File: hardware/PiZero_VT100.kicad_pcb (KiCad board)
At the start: 2 copper layers, 99.8 x 100.1 mm, 41 parts, among them J1 GPIO, J2 RS232, J3 Ext. Power max,. 9V DC/AC, J4 Mini-DIN-6, J5 to Testpins 22(DM) and TP23(D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, J6 USB_A, J7 Z80-MBC2 direct, J8 LCD Power, J9 On / Off, K1 G5V-2, Q1 BC546, Q2 BC546, U1 LM350_TO220

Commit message: small changes, typos
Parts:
- moved J8 38.6 mm to (136.7, 118.1), turned to 0 degrees
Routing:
- net +5V: track 295.6 -> 299.7 mm
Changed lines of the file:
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@@
 		(grid_origin 99.2 168.6)
 		(pcbplotparams
-			(layerselection 0x00000000_00000000_55555555_57555554)
+			(layerselection 0x00000000_00000000_5555555d_df55557f)
 			(plot_on_all_layers_selection 0x00000000_00000000_00000000_00000000)
 			(disableapertmacros no)
@@
 	(footprint "Connector_PinHeader_2.54mm:PinHeader_1x02_P2.54mm_Vertical"
 		(layer "F.Cu")
-		(at 105.775 95 -90)
+		(at 136.7 118.075)
 		(descr "Through hole straight pin header, 1x02, 2.54mm pitch, single row")
 		(tags "Through hole pin header THT 1x02 2.54mm single row")
 		(property "Reference" "J8"
-			(at 0 -2.38 90)
+			(at 0 -2.38 0)
 			(layer "F.SilkS")
 			(effects
@@
 		)
 		(property "Value" "LCD Power"
-			(at -3.5 0.775 180)
+			(at -3.5 0.775 90)
 			(layer "F.Fab")
 			(effects
@@
 		)
 		(property "Datasheet" ""
-			(at 0 0 90)
+			(at 0 0 0)
 			(layer "F.Fab")
 			(hide yes)
@@
 		)
 		(property "Description" "Generic connector, single row, 01x02, script generated"
-			(at 0 0 90)
+			(at 0 0 0)
 			(layer "F.Fab")
 			(hide yes)
@@
 		(attr through_hole)
 		(fp_line
-			(start -1.38 3.92)
-			(end 1.38 3.92)
+			(start -1.38 -1.38)
+			(end 0 -1.38)
 			(stroke
 				(width 0.12)
@@
 		)
 		(fp_line
-			(start -1.38 1.27)
-			(end -1.38 3.92)
+			(start -1.38 0)
+			(end -1.38 -1.38)
 			(stroke
 				(width 0.12)
@@
 		(fp_line
 			(start -1.38 1.27)
-			(end 1.38 1.27)
+			(end -1.38 3.92)
 			(stroke
 				(width 0.12)
@@
 		)
 		(fp_line
-			(start 1.38 1.27)
-			(end 1.38 3.92)
+			(start -1.38 1.27)
+			(end 1.38 1.27)
 			(stroke
 				(width 0.12)
@@
 		)
 		(fp_line
-			(start -1.38 0)
-			(end -1.38 -1.38)
+			(start -1.38 3.92)
+			(end 1.38 3.92)
 			(stroke
 				(width 0.12)
@@
 		)
 		(fp_line
-			(start -1.38 -1.38)
-			(end 0 -1.38)
+			(start 1.38 1.27)
+			(end 1.38 3.92)
 			(stroke
 				(width 0.12)
@@
 		)
 		(fp_line
-			(start -1.77 4.32)
-			(end 1.77 4.32)
+			(start -1.77 -1.77)
+			(end -1.77 4.32)
 			(stroke
 				(width 0.05)
@@
 		)
 		(fp_line
-			(start 1.77 4.32)
-			(end 1.77 -1.77)
+			(start -1.77 4.32)
+			(end 1.77 4.32)
 			(stroke
 				(width 0.05)
@@
 		)
 		(fp_line
-			(start -1.77 -1.77)
-			(end -1.77 4.32)
+			(start 1.77 -1.77)
+			(end -1.77 -1.77)
 			(stroke
 				(width 0.05)
@@
 		)
 		(fp_line
-			(start 1.77 -1.77)
-			(end -1.77 -1.77)
+			(start 1.77 4.32)
+			(end 1.77 -1.77)
 			(stroke
 				(width 0.05)
@@
 		)
 		(fp_line
-			(start -1.27 3.81)
-			(end -1.27 -0.635)
+			(start -1.27 -0.635)
+			(end -0.635 -1.27)
 			(stroke
 				(width 0.1)
@@
 		)
 		(fp_line
-			(start 1.27 3.81)
-			(end -1.27 3.81)
+			(start -1.27 3.81)
+			(end -1.27 -0.635)
 			(stroke
 				(width 0.1)
@@
 		)
 		(fp_line
-			(start -1.27 -0.635)
-			(end -0.635 -1.27)
+			(start -0.635 -1.27)
+			(end 1.27 -1.27)
 			(stroke
 				(width 0.1)
@@
 		)
 		(fp_line
-			(start -0.635 -1.27)
-			(end 1.27 -1.27)
+			(start 1.27 -1.27)
+			(end 1.27 3.81)
 			(stroke
 				(width 0.1)
@@
 		)
 		(fp_line
-			(start 1.27 -1.27)
-			(end 1.27 3.81)
+			(start 1.27 3.81)
+			(end -1.27 3.81)
 			(stroke
 				(width 0.1)
@@
 		)
 		(fp_text user "${REFERENCE}"
-			(at 0 1.27 0)
+			(at 0 1.27 90)
 			(layer "F.Fab")
 			(effects
@@
 		)
 		(pad "1" thru_hole rect
-			(at 0 0 270)
+			(at 0 0)
 			(size 1.7 1.7)
 			(drill 1)
@@
 		)
 		(pad "2" thru_hole circle
-			(at 0 2.54 270)
+			(at 0 2.54)
 			(size 1.7 1.7)
 			(drill 1)
@@
 	)
 	(segment
+		(start 136.7 118.075)
+		(end 127.125 118.075)
+		(width 0.8)
+		(layer "B.Cu")
+		(net 30)
+	)
+	(segment
 		(start 135.91 148.05)
 		(end 130.96 143.1)
@@
 	)
 	(segment
-		(start 127 120)
+		(start 127 117.95)
 		(end 127 113.2)
 		(width 0.8)
@@
 	)
 	(segment
-		(start 105.775 98.942677)
-		(end 107 100.167677)
-		(width 0.8)
-		(layer "B.Cu")
-		(net 30)
-	)
-	(segment
 		(start 193 98)
 		(end 192 97)
@@
 	)
 	(segment
+		(start 127 120)
+		(end 127 117.95)
+		(width 0.8)
+		(layer "B.Cu")
+		(net 30)
+	)
+	(segment
 		(start 121.4 119.96)
 		(end 126.96 119.96)
@@
 	)
 	(segment
-		(start 105.775 95)
-		(end 105.775 98.942677)
+		(start 127.125 118.075)
+		(end 127 117.95)
 		(width 0.8)
 		(layer "B.Cu")

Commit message: Analyzing VT100 support and extension
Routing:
- net Net-(J3-Ext): track 14.8 -> 24.8 mm
- net +5V: track 299.7 -> 299.0 mm
- added copper zone on F.Cu, net GND
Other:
- board size 99.8 x 100.1 mm -> 99.7 x 99.6 mm
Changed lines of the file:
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@@
 			)
 		)
-		(pad "1" thru_hole circle
+		(pad "1" thru_hole rect
 			(at 0 0)
-			(size 2 2)
-			(drill 1.2)
+			(size 4.6 2)
+			(drill oval 3.6 1)
 			(layers "*.Cu" "*.Mask")
 			(remove_unused_layers no)
@@
 			(pintype "passive")
 		)
-		(pad "2" thru_hole circle
+		(pad "2" thru_hole oval
 			(at 0 6.3)
-			(size 2 2)
-			(drill 1.2)
+			(size 4.2 2)
+			(drill oval 3.2 1)
 			(layers "*.Cu" "*.Mask")
 			(remove_unused_layers no)
@@
 		(pad "3" thru_hole oval
 			(at 4.8 2.9)
-			(size 2 2)
-			(drill 1.2)
+			(size 2 4.2)
+			(drill oval 1 3.2)
 			(layers "*.Cu" "*.Mask")
 			(remove_unused_layers no)
@@
 	(gr_poly
 		(pts
-			(xy 99.15 68.5) (xy 198.95 68.5) (xy 198.95 168.55) (xy 187.498724 168.452955) (xy 187.548743 160.5)
+			(xy 99.1502 68.9) (xy 198.85 68.9) (xy 198.85 168.549152) (xy 187.498724 168.452955) (xy 187.548743 160.5)
 			(xy 173.5 160.5) (xy 173.50092 168.45) (xy 99.2 168.45)
 		)
@@
 	)
 	(segment
-		(start 106.917677 100.25)
-		(end 107.5 100.25)
-		(width 0.8)
-		(layer "B.Cu")
-		(net 30)
-	)
-	(segment
 		(start 192 97)
 		(end 183.5 97)
@@
 	)
 	(segment
-		(start 107 100.167677)
-		(end 106.917677 100.25)
-		(width 0.8)
-		(layer "B.Cu")
-		(net 30)
-	)
-	(segment
 		(start 112.5 143.5)
 		(end 109.5 146.5)
@@
 	)
 	(segment
-		(start 111.75 158.8)
-		(end 114.1 156.45)
+		(start 114.1 147.48)
+		(end 114.58 147)
 		(width 0.8)
 		(layer "B.Cu")
@@
 	)
 	(segment
-		(start 114.1 147.48)
-		(end 114.58 147)
+		(start 111.85 160.7)
+		(end 111.75 160.6)
+		(width 0.8)
+		(layer "B.Cu")
+		(net 36)
+	)
+	(segment
+		(start 114.58 147)
+		(end 115.5 147)
 		(width 0.8)
 		(layer "B.Cu")
@@
 	)
 	(segment
-		(start 111.75 160.6)
-		(end 111.75 158.8)
+		(start 115.5 147)
+		(end 119.55 151.05)
 		(width 0.8)
 		(layer "B.Cu")
@@
 	)
 	(segment
-		(start 114.1 156.45)
-		(end 114.1 147.48)
+		(start 119.55 151.05)
+		(end 119.55 160.7)
+		(width 0.8)
+		(layer "B.Cu")
+		(net 36)
+	)
+	(segment
+		(start 119.55 160.7)
+		(end 111.85 160.7)
 		(width 0.8)
 		(layer "B.Cu")
@@
 		(net 1)
 		(net_name "GND")
-		(layer "B.Cu")
+		(layers "F.Cu" "B.Cu")
 		(hatch edge 0.5)
 		(connect_pads yes
@@
 		(polygon
 			(pts
-				(xy 99 68.5) (xy 199 68.5) (xy 199 168.5) (xy 99 168.5)
+				(xy 99 69.05) (xy 198.95 69.05) (xy 198.95 168.5) (xy 99 168.5)
 			)
 		)

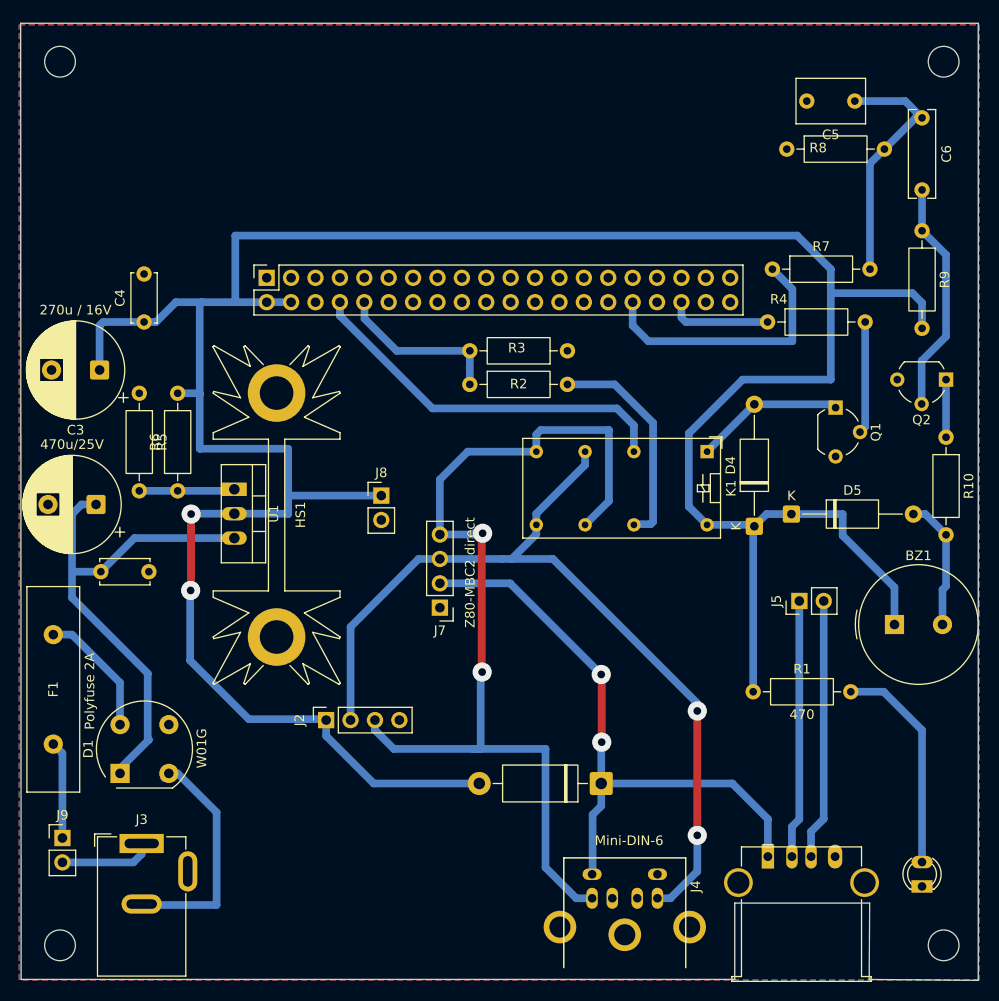
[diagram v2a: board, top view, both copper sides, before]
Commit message: Adapterplatine V2.0 mit Schaltregler. da Linearregler zu hohe Wärmeentwicklung hat
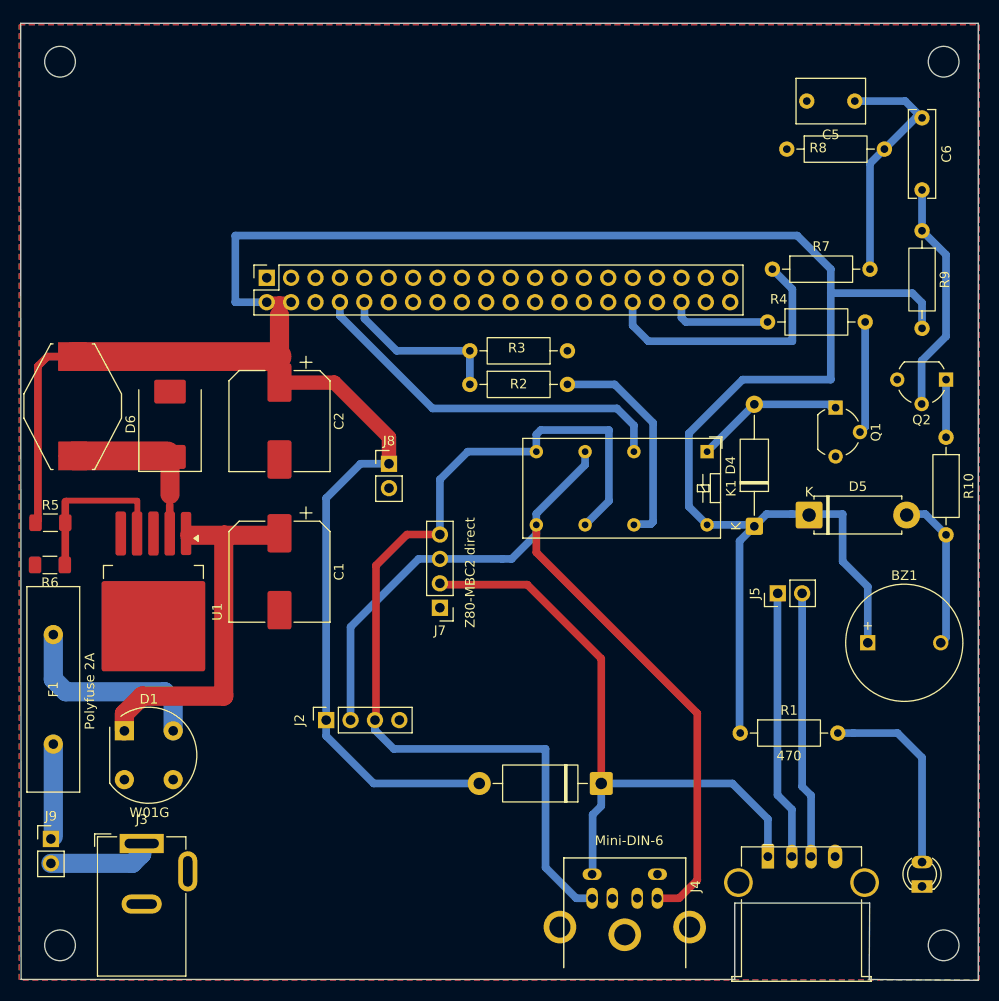
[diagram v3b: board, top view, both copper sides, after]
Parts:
- removed C3: 270u / 16V, Capacitor_THT:CP_Radial_D10.0mm_P5.00mm
- removed C4: 0,1u, Capacitor_THT:C_Disc_D5.0mm_W2.5mm_P5.00mm
- removed HS1: 6 K/W, Heatsink:Heatsink_Fischer_SK104-STCB_35x13mm__2xDrill3.5mm_ScrewM3
- added D6: MBRS340, Diode_SMD:D_SMC, F.Cu at (114.7, 110.7)
- added L1: 90U, Inductor_SMD:L_Fastron_PISN, F.Cu at (104.6, 108.8)
- BZ1: footprint Buzzer_Beeper:Buzzer_TDK_PS1240P02BT_D12.2mm_H6.5mm -> Buzzer_Beeper:MagneticBuzzer_ProSignal_ABI-009-RC
- C1: value 470u/25V -> 470u; footprint Capacitor_THT:CP_Radial_D10.0mm_P5.00mm -> Capacitor_SMD:CP_Elec_10x10
- C2: value 0,1u -> 470u / 25V; footprint Capacitor_THT:C_Disc_D5.0mm_W2.5mm_P5.00mm -> Capacitor_SMD:CP_Elec_10x10
- D5: value 1N4148 -> D; footprint Diode_THT:D_A-405_P12.70mm_Horizontal -> Diode_THT:D_5W_P10.16mm_Horizontal
- R5: value 680 -> 10k; footprint Resistor_THT:R_Axial_DIN0207_L6.3mm_D2.5mm_P10.16mm_Horizontal -> Resistor_SMD:R_1206_3216Metric_Pad1.30x1.75mm_HandSolder
- R6: value 220 -> 3.2k; footprint Resistor_THT:R_Axial_DIN0207_L6.3mm_D2.5mm_P10.16mm_Horizontal -> Resistor_SMD:R_1206_3216Metric_Pad1.30x1.75mm_HandSolder
- U1: value LM350_TO220 -> LM2576HVS-ADJ; footprint Package_TO_SOT_THT:TO-220-3_Vertical -> Package_TO_SOT_SMD:TO-263-5_TabPin3
- moved C2 24.3 mm to (126.1, 110.3), turned to -90 degrees
- moved C1 20.3 mm to (126.1, 126.0), turned to -90 degrees
- moved R5 16.3 mm to (102.2, 120.9), turned to 0 degrees
- moved R6 15.4 mm to (102.2, 125.3), turned to 180 degrees
- moved U1 15.3 mm to (113.0, 130.2)
- moved R1 4.51 mm to (174.1, 142.8)
- moved D1 4.45 mm to (110.0, 142.6), turned to 0 degrees
- moved J8 3.41 mm to (137.5, 114.8)
- moved BZ1 3.37 mm to (187.3, 133.4)
- moved J5 2.39 mm to (178.0, 128.2)
- moved D5 1.84 mm to (181.2, 120.1)
- moved J9 1.20 mm to (102.3, 153.8)
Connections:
- C2 pad 1: Net-(D1-+) -> +5V
- D1 pad 2: Net-(J3-Ext) -> GND
- J3 pad 2: Net-(J3-Ext) -> GND
- R5 pad 1: GND -> +5V
- R5 pad 2: Net-(U1-ADJ) -> Net-(U1-FB)
- R6 pad 1: Net-(U1-ADJ) -> Net-(U1-FB)
- R6 pad 2: +5V -> GND
- U1 pad 1: Net-(U1-ADJ) -> Net-(D1-+)
- U1 pad 2: +5V -> Net-(D6-K)
- U1 pad 3: Net-(D1-+) -> GND
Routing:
- net Net-(J3-Ext): track 24.8 -> 0.00 mm
- net Net-(U1-FB): track 0.00 -> 18.1 mm
- net Net-(D6-K): track 0.00 -> 17.4 mm
- net Net-(D1-+): track 52.3 -> 39.1 mm
- net Net-(U1-ADJ): track 9.97 -> 0.00 mm
- net Net-(D1-Pad4): track 13.4 -> 21.2 mm
- net Net-(J2-Pin_3): track 103.4 -> 99.7 mm, vias 2 -> 0
- net Net-(D2-A): track 22.8 -> 20.7 mm
- net Net-(BZ1--): track 13.8 -> 15.8 mm
- net Net-(J3-In): track 9.71 -> 10.9 mm
- net Net-(J5-Pin_1): track 26.9 -> 28.0 mm
- net Net-(D3-K): track 64.8 -> 65.7 mm, vias 2 -> 0
- net Net-(J5-Pin_2): track 27.2 -> 27.8 mm
- net +5V: track 299.0 -> 299.5 mm, vias 2 -> 0
- net Net-(J2-Pin_2): track 92.2 -> 92.6 mm, vias 2 -> 0

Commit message: PCB Adapterboard geändert
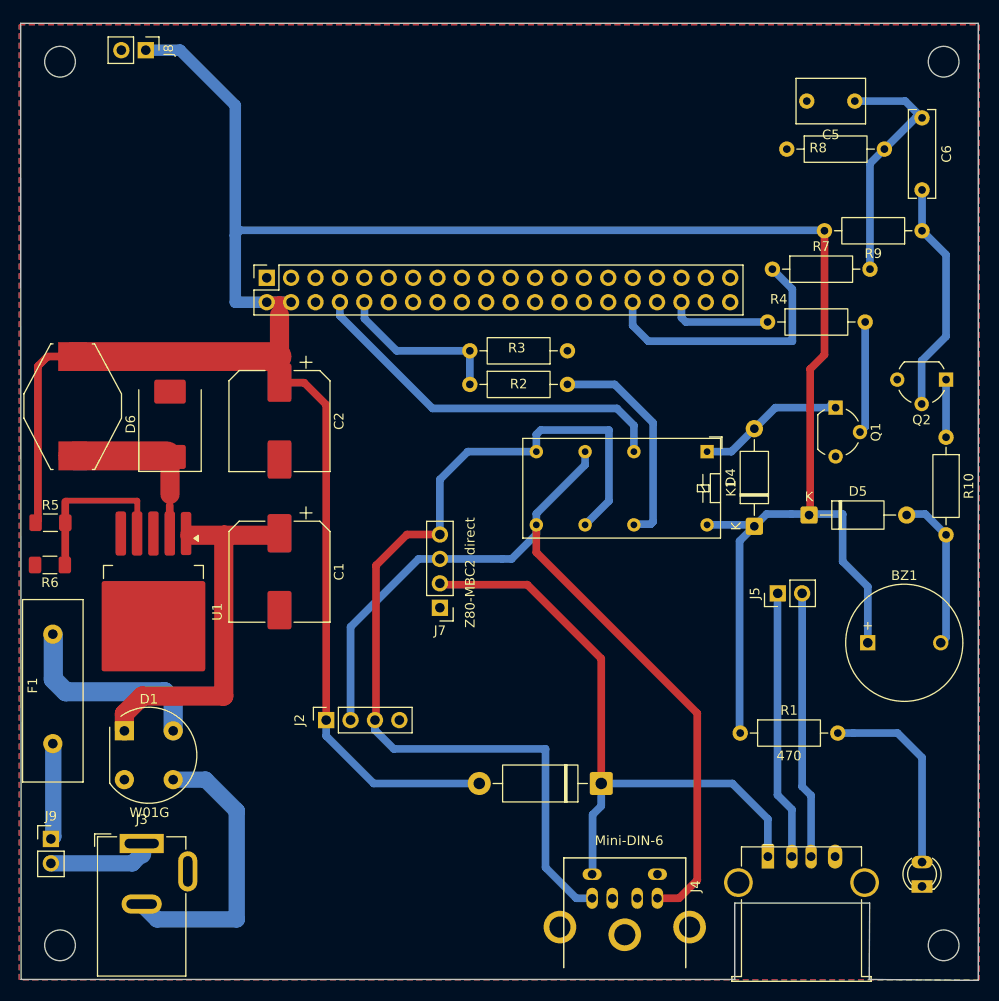
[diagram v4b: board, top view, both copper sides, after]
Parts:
- D4: footprint Diode_THT:D_A-405_P12.70mm_Horizontal -> Diode_THT:D_A-405_P10.16mm_Horizontal
- D5: footprint Diode_THT:D_5W_P10.16mm_Horizontal -> Diode_THT:D_A-405_P10.16mm_Horizontal
- F1: footprint Fuse:Fuse_Littelfuse-LVR125 -> Fuse:Fuse_Littelfuse-LVR200
- L1: value 90U -> 47u
- R5: value 10k -> 12k
- R6: value 3.2k -> 3,9k
- moved J8 50.0 mm to (112.2, 71.7), turned to -90 degrees
- moved F1 0.07 mm to (102.5, 143.9)
- turned R9 to 180 degrees
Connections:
- D1 pad 3: GND -> Net-(D1--)
- J3 pad 2: GND -> Net-(D1--)
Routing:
- net Net-(D1--): track 0.00 -> 29.8 mm
- net +5V: track 299.5 -> 292.7 mm
